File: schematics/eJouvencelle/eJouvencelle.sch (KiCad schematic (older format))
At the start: 19 parts

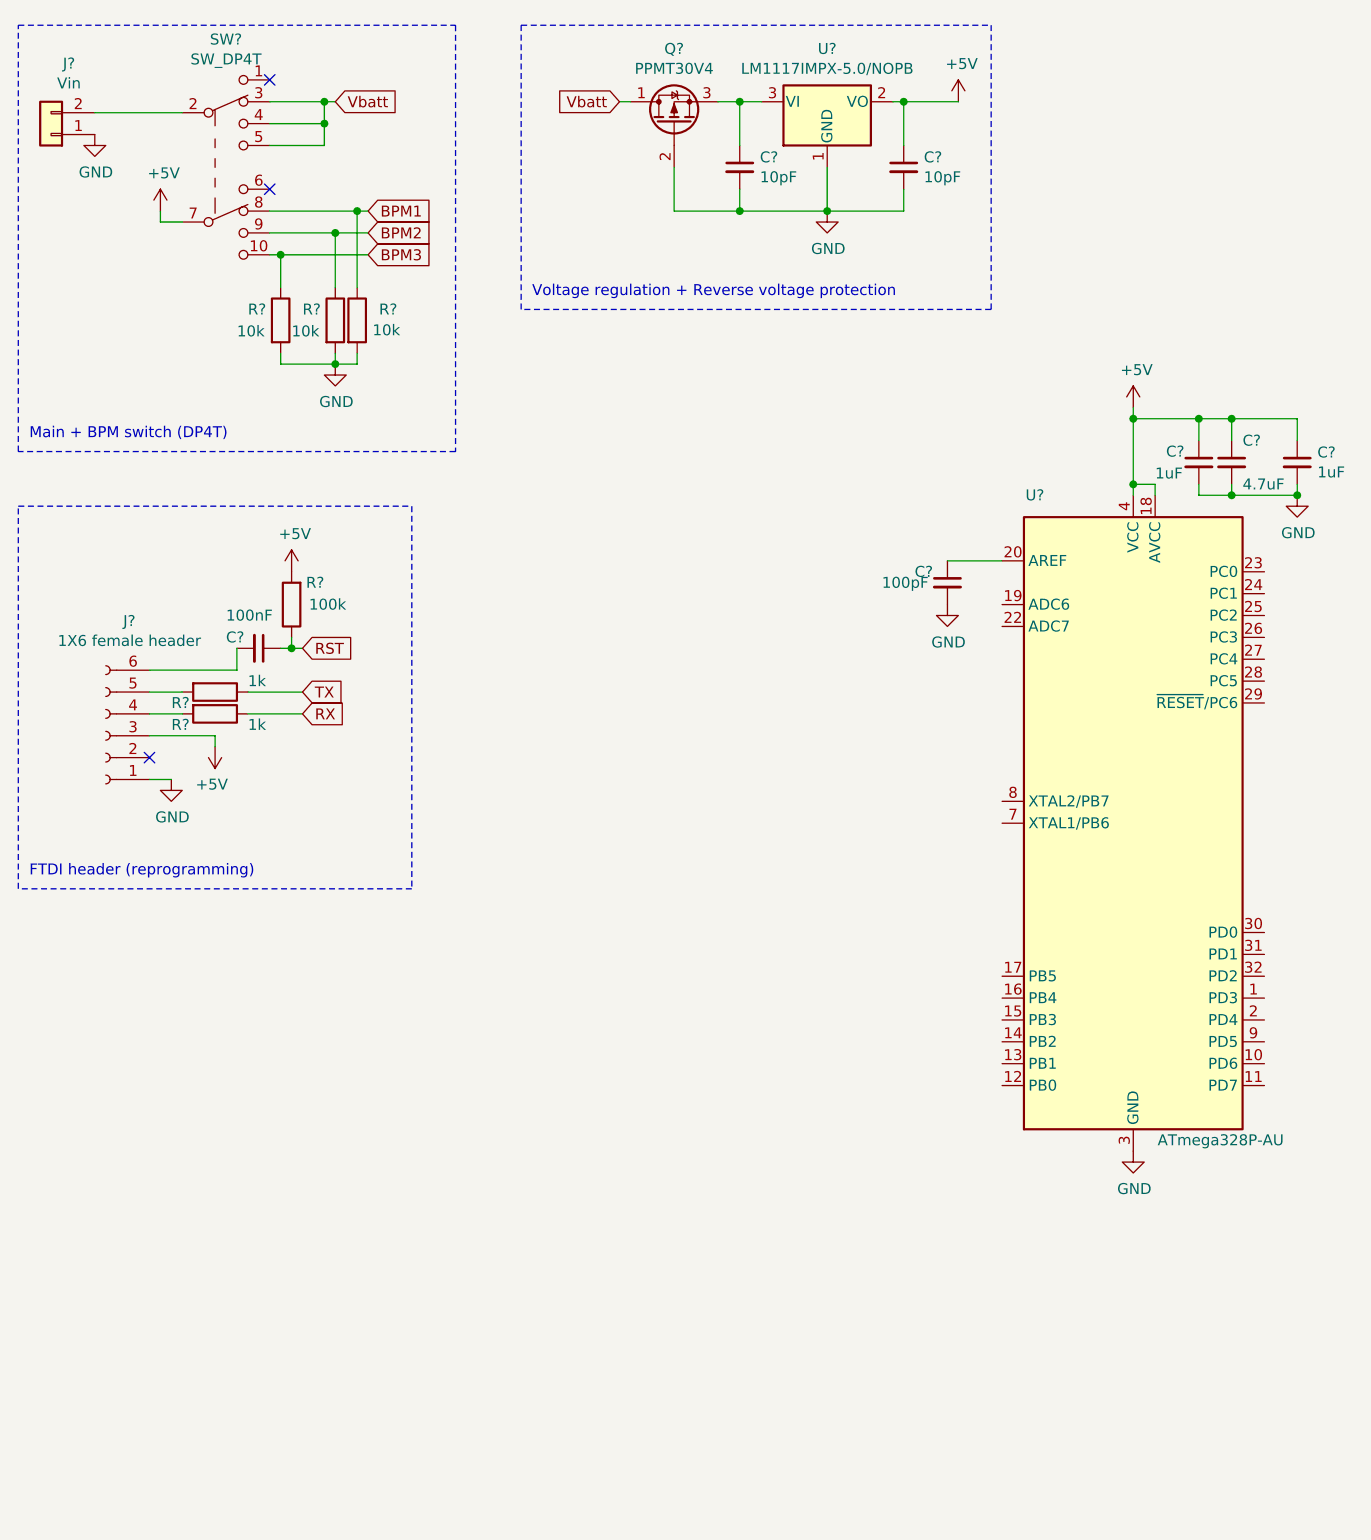
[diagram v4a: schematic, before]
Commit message: move reverse voltage protection before main switch
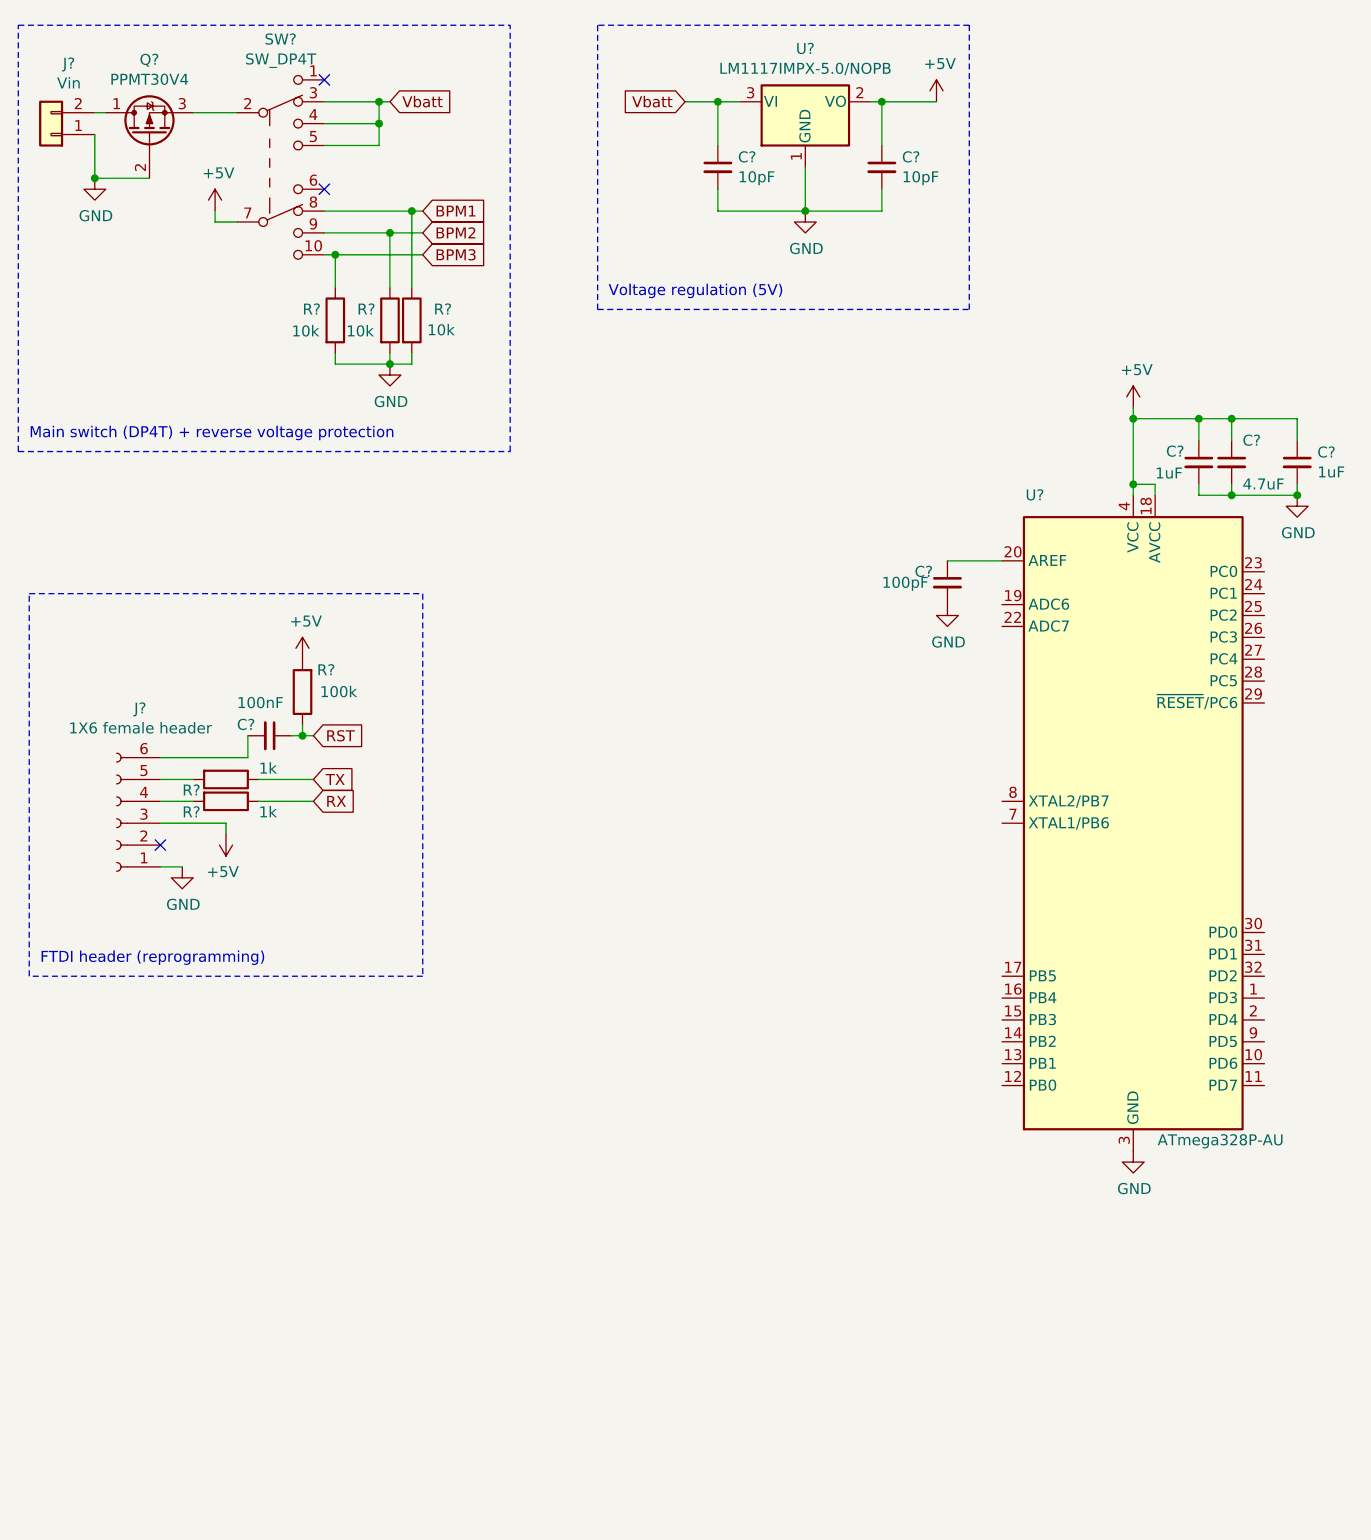
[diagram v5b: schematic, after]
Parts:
- removed Q?: PPMT30V4, symbol Device:Q_PMOS_DGS
- added Q?: PPMT30V4, symbol Device:Q_PMOS_DGS
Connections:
- net GND: now also Q?.2 (G)
- net Vbatt: now also C?.1, U?.3 (VI)
- net at SW?.2 (B): now also Q?.3 (S); no longer J?.2 (Pin_2)
- new net: J?.2 (Pin_2), Q?.1 (D)
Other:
- note added: "Main switch (DP4T) + reverse voltage protection"
- note added: "Voltage regulation (5V)"
- note removed: "Main + BPM switch (DP4T)"
- note removed: "Voltage regulation + Reverse voltage protection"
- moved on the sheet: C?, J?, R?, SW?, U?

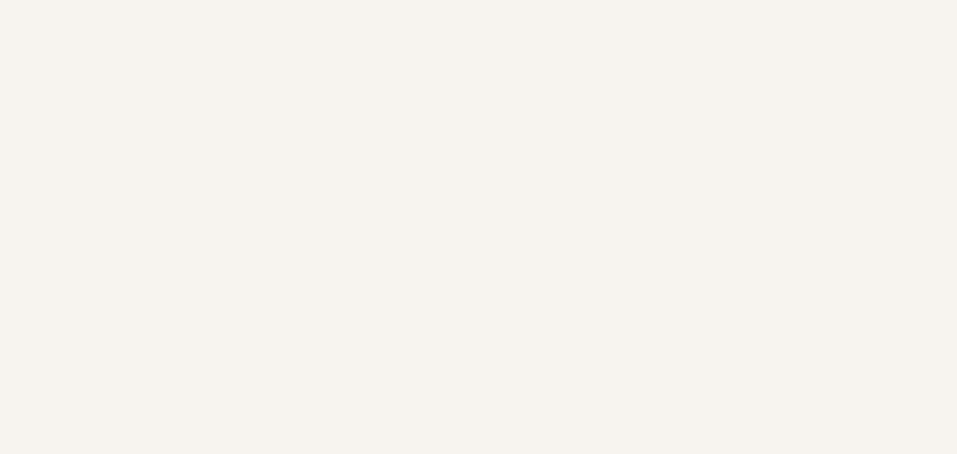
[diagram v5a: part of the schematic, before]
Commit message: add buttons w/ debouncing
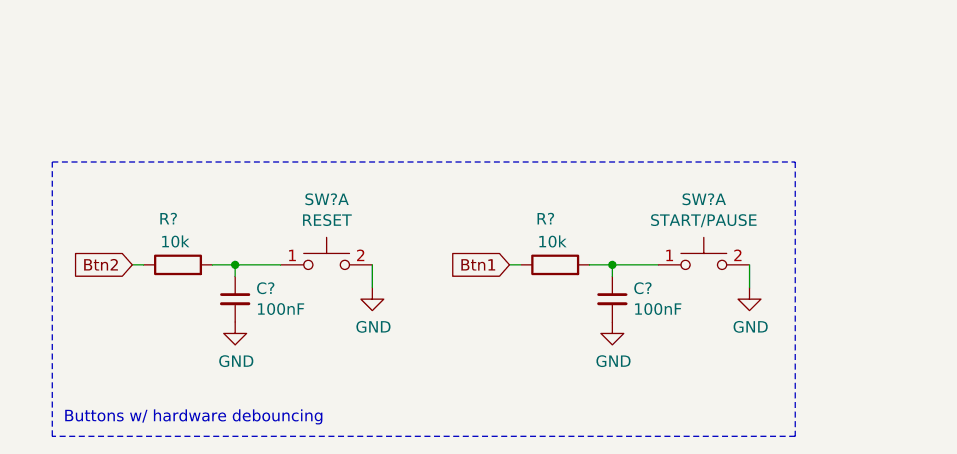
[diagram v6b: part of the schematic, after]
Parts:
- added C? (x2): 100nF, symbol Device:C_Small
- added R? (x2): 10k, symbol Device:R
- added SW?: START/PAUSE, symbol Switch:SW_Push_Dual_x2
- added SW?: RESET, symbol Switch:SW_Push_Dual_x2
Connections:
- net GND: now also C?.2, C?.2, SW?.2 (D), SW?.2 (D)
- new net: C?.1, R?.2, SW?.1 (C) (x2)
- new net Btn1: R?.1
- new net Btn2: R?.1
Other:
- note added: "Buttons w/ hardware debouncing"
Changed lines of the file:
@@
 Wire Notes Line
 	3300 1900 5000 1900
+$Comp
+L Switch:SW_Push_Dual_x2 SW?
+U 1 1 5E988120
+P 3650 6700
+F 0 "SW?" H 3650 6985 50  0000 C CNN
+F 1 "START/PAUSE" H 3650 6894 50  0000 C CNN
+F 2 "" H 3650 6900 50  0001 C CNN
+F 3 "~" H 3650 6900 50  0001 C CNN
+	1    3650 6700
+	1    0    0    -1
+$EndComp
+$Comp
+L power:GND #PWR?
+U 1 1 5E9886EF
+P 3850 6800
+F 0 "#PWR?" H 3850 6550 50  0001 C CNN
+F 1 "GND" H 3855 6627 50  0000 C CNN
+F 2 "" H 3850 6800 50  0001 C CNN
+F 3 "" H 3850 6800 50  0001 C CNN
+	1    3850 6800
+	1    0    0    -1
+$EndComp
+$Comp
+L power:GND #PWR?
+U 1 1 5E9894CA
+P 3250 6950
+F 0 "#PWR?" H 3250 6700 50  0001 C CNN
+F 1 "GND" H 3255 6777 50  0000 C CNN
+F 2 "" H 3250 6950 50  0001 C CNN
+F 3 "" H 3250 6950 50  0001 C CNN
+	1    3250 6950
+	1    0    0    -1
+$EndComp
+$Comp
+L Device:C_Small C?
+U 1 1 5E98A244
+P 3250 6850
+F 0 "C?" H 3342 6896 50  0000 L CNN
+F 1 "100nF" H 3342 6805 50  0000 L CNN
+F 2 "" H 3250 6850 50  0001 C CNN
+F 3 "~" H 3250 6850 50  0001 C CNN
+	1    3250 6850
+	1    0    0    -1
+$EndComp
+$Comp
+L Device:R R?
+U 1 1 5E98C381
+P 3000 6700
+F 0 "R?" V 3200 6700 50  0000 L CNN
+F 1 "10k" V 3100 6650 50  0000 L CNN
+F 2 "" V 2930 6700 50  0001 C CNN
+F 3 "~" H 3000 6700 50  0001 C CNN
+	1    3000 6700
+	0    -1   -1   0
+$EndComp
+Text GLabel 2800 6700 0    50   Input ~ 0
+Btn1
+Wire Wire Line
+	3850 6700 3850 6800
+Wire Wire Line
+	3450 6700 3250 6700
+Wire Wire Line
+	3250 6750 3250 6700
+Connection ~ 3250 6700
+Wire Wire Line
+	3250 6700 3150 6700
+Wire Wire Line
+	2850 6700 2800 6700
+$Comp
+L Switch:SW_Push_Dual_x2 SW?
+U 1 1 5E9A157F
+P 2000 6700
+F 0 "SW?" H 2000 6985 50  0000 C CNN
+F 1 "RESET" H 2000 6894 50  0000 C CNN
+F 2 "" H 2000 6900 50  0001 C CNN
+F 3 "~" H 2000 6900 50  0001 C CNN
+	1    2000 6700
+	1    0    0    -1
+$EndComp
+$Comp
+L power:GND #PWR?
+U 1 1 5E9A1585
+P 2200 6800
+F 0 "#PWR?" H 2200 6550 50  0001 C CNN
+F 1 "GND" H 2205 6627 50  0000 C CNN
+F 2 "" H 2200 6800 50  0001 C CNN
+F 3 "" H 2200 6800 50  0001 C CNN
+	1    2200 6800
+	1    0    0    -1
+$EndComp
+$Comp
+L power:GND #PWR?
+U 1 1 5E9A158B
+P 1600 6950
+F 0 "#PWR?" H 1600 6700 50  0001 C CNN
+F 1 "GND" H 1605 6777 50  0000 C CNN
+F 2 "" H 1600 6950 50  0001 C CNN
+F 3 "" H 1600 6950 50  0001 C CNN
+	1    1600 6950
+	1    0    0    -1
+$EndComp
+$Comp
+L Device:C_Small C?
+U 1 1 5E9A1591
+P 1600 6850
+F 0 "C?" H 1692 6896 50  0000 L CNN
+F 1 "100nF" H 1692 6805 50  0000 L CNN
+F 2 "" H 1600 6850 50  0001 C CNN
+F 3 "~" H 1600 6850 50  0001 C CNN
+	1    1600 6850
+	1    0    0    -1
+$EndComp
+$Comp
+L Device:R R?
+U 1 1 5E9A1597
+P 1350 6700
+F 0 "R?" V 1550 6700 50  0000 L CNN
+F 1 "10k" V 1450 6650 50  0000 L CNN
+F 2 "" V 1280 6700 50  0001 C CNN
+F 3 "~" H 1350 6700 50  0001 C CNN
+	1    1350 6700
+	0    -1   -1   0
+$EndComp
+Text GLabel 1150 6700 0    50   Input ~ 0
+Btn2
+Wire Wire Line
+	2200 6700 2200 6800
+Wire Wire Line
+	1800 6700 1600 6700
+Wire Wire Line
+	1600 6750 1600 6700
+Connection ~ 1600 6700
+Wire Wire Line
+	1600 6700 1500 6700
+Wire Wire Line
+	1200 6700 1150 6700
+Wire Notes Line
+	4050 6250 4050 7450
+Wire Notes Line
+	4050 7450 800  7450
+Wire Notes Line
+	800  7450 800  6250
+Wire Notes Line
+	800  6250 4050 6250
+Text Notes 850  7400 0    50   ~ 0
+Buttons w/ hardware debouncing
 $EndSCHEMATC

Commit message: add labels to atmega
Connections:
- net BPM1: now also U?.15 (PB3)
- net BPM2: now also U?.17 (PB5)
- net BPM3: now also U?.2 (PD4)
- net Btn1: now also U?.32 (PD2)
- net Btn2: now also U?.1 (PD3)
- net RST: now also U?.29 (~RESET~/PC6)
- net RX: now also U?.30 (PD0)
- net TX: now also U?.31 (PD1)
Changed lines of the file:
@@
 Text Notes 850  7400 0    50   ~ 0
 Buttons w/ hardware debouncing
+Text GLabel 6400 5050 2    50   Input ~ 0
+Btn2
+Text GLabel 6400 4950 2    50   Input ~ 0
+Btn1
+Text GLabel 6400 4850 2    50   Input ~ 0
+TX
+Text GLabel 6400 4750 2    50   Input ~ 0
+RX
+Text GLabel 6400 3700 2    50   Input ~ 0
+RST
+Text GLabel 6400 5150 2    50   Input ~ 0
+BPM3
+Text GLabel 5100 5150 0    50   Input ~ 0
+BPM1
+Text GLabel 5100 4950 0    50   Input ~ 0
+BPM2
+Wire Wire Line
+	6400 3700 6350 3700
+Wire Wire Line
+	6400 4750 6350 4750
+Wire Wire Line
+	6400 4850 6350 4850
+Wire Wire Line
+	6350 4950 6400 4950
+Wire Wire Line
+	6400 5050 6350 5050
+Wire Wire Line
+	6350 5150 6400 5150
+Wire Wire Line
+	5150 5150 5100 5150
+Wire Wire Line
+	5100 4950 5150 4950
 $EndSCHEMATC

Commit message: add 16MHz crystal oscillator
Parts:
- added C? (x2): 22pF, symbol Device:C_Small
- added Y?: 16MHz, symbol Device:Crystal_Small
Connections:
- net GND: now also C?.2, C?.2
- net at U?.7 (XTAL1/PB6): now also C?.1, Y?.2
- net at U?.8 (XTAL2/PB7): now also C?.1, Y?.1
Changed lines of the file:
@@
 Wire Wire Line
 	5100 4950 5150 4950
+$Comp
+L Device:Crystal_Small Y?
+U 1 1 5E9C7E98
+P 4800 4200
+F 0 "Y?" H 4800 4425 50  0000 C CNN
+F 1 "16MHz" H 4800 4334 50  0000 C CNN
+F 2 "" H 4800 4200 50  0001 C CNN
+F 3 "~" H 4800 4200 50  0001 C CNN
+	1    4800 4200
+	0    1    1    0
+$EndComp
+$Comp
+L Device:C_Small C?
+U 1 1 5E9C9A95
+P 4700 4050
+F 0 "C?" V 4450 4000 50  0000 L CNN
+F 1 "22pF" V 4550 4000 50  0000 L CNN
+F 2 "" H 4700 4050 50  0001 C CNN
+F 3 "~" H 4700 4050 50  0001 C CNN
+	1    4700 4050
+	0    1    1    0
+$EndComp
+$Comp
+L Device:C_Small C?
+U 1 1 5E9CA38F
+P 4700 4350
+F 0 "C?" V 4800 4300 50  0000 L CNN
+F 1 "22pF" V 4900 4300 50  0000 L CNN
+F 2 "" H 4700 4350 50  0001 C CNN
+F 3 "~" H 4700 4350 50  0001 C CNN
+	1    4700 4350
+	0    1    1    0
+$EndComp
+$Comp
+L power:GND #PWR?
+U 1 1 5E9CA80F
+P 4600 4200
+F 0 "#PWR?" H 4600 3950 50  0001 C CNN
+F 1 "GND" H 4605 4027 50  0000 C CNN
+F 2 "" H 4600 4200 50  0001 C CNN
+F 3 "" H 4600 4200 50  0001 C CNN
+	1    4600 4200
+	0    1    1    0
+$EndComp
+Wire Wire Line
+	4800 4350 4800 4300
+Wire Wire Line
+	4800 4100 4800 4050
+Wire Wire Line
+	4600 4050 4600 4200
+Connection ~ 4600 4200
+Wire Wire Line
+	4600 4200 4600 4350
+Wire Wire Line
+	5100 4350 4800 4350
+Connection ~ 4800 4350
+Wire Wire Line
+	5100 4050 4800 4050
+Connection ~ 4800 4050
+Wire Wire Line
+	5100 4050 5100 4150
+Wire Wire Line
+	5100 4350 5100 4250
+Wire Wire Line
+	5100 4150 5150 4150
+Wire Wire Line
+	5100 4250 5150 4250
 $EndSCHEMATC
